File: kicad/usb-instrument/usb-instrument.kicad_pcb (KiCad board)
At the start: 4 copper layers, 100 x 100 mm, 74 parts, among them J1 USB_B_Micro, J2 USB_C_Receptacle_USB2.0_14P, Q5 BS170, Q6 BSS84, Q7 BS170, Q8 BS170, U1 XIAO-ESP32-C3-DIP, U12 LM321, U13 LM321, U2 ADS131M02IRUKR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

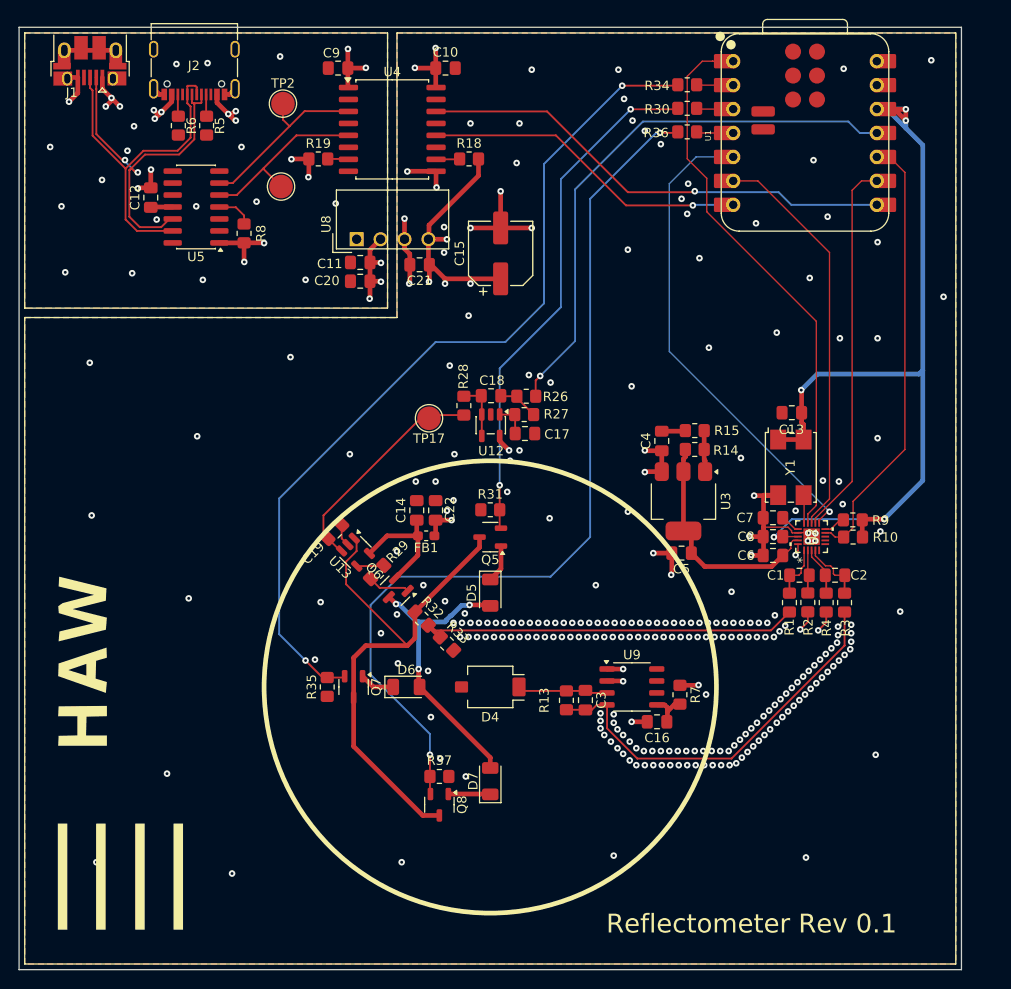
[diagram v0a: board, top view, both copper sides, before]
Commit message: updated footprints
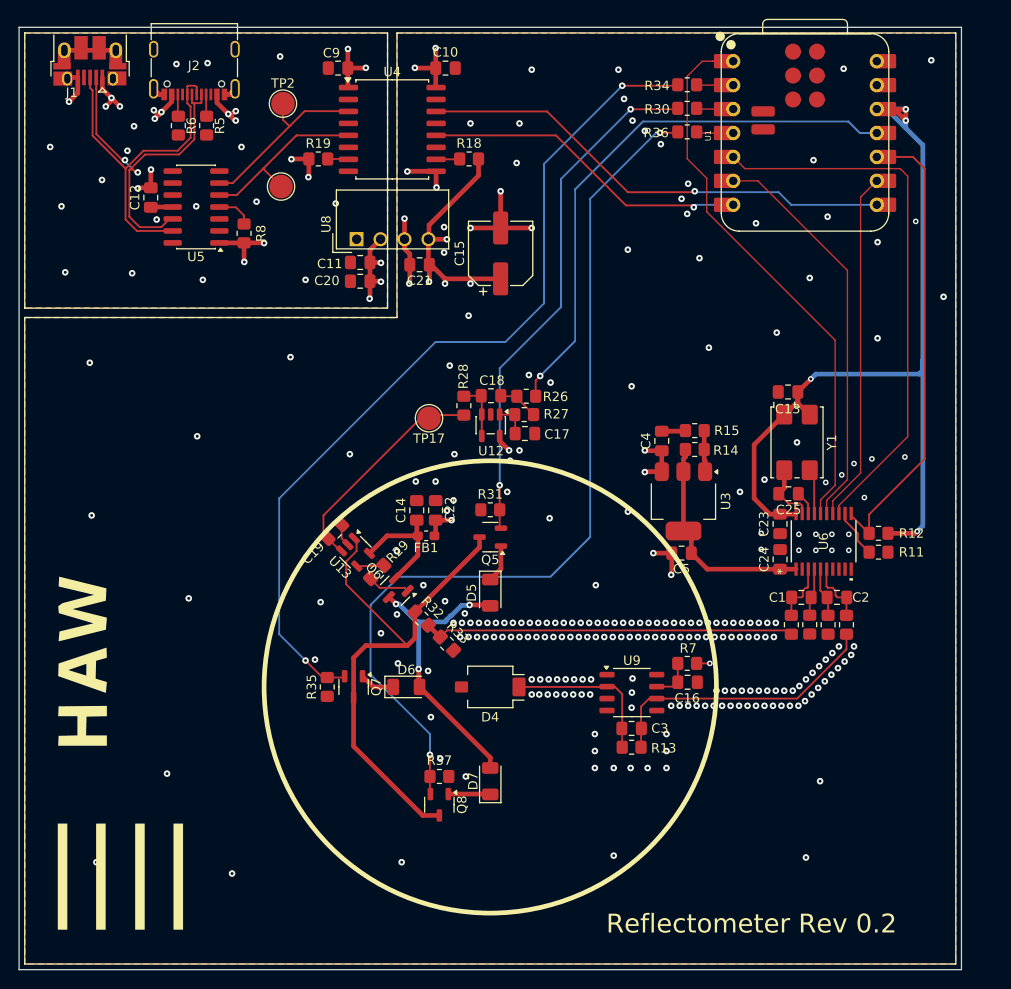
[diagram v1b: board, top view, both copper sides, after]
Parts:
- removed C6, C8: 1u, Capacitor_SMD:C_0805_2012Metric_Pad1.18x1.45mm_HandSolder
- removed C7: 220n, Capacitor_SMD:C_0805_2012Metric_Pad1.18x1.45mm_HandSolder
- removed R10, R9: 10k, Resistor_SMD:R_0805_2012Metric_Pad1.20x1.40mm_HandSolder
- removed U2: ADS131M02IRUKR, Footprints:WQFN20_ADS131_TEX
- added C23: 1u, Capacitor_SMD:C_0805_2012Metric_Pad1.18x1.45mm_HandSolder, F.Cu at (130.8, 102.7)
- added C24: 1u, Capacitor_SMD:C_0805_2012Metric_Pad1.18x1.45mm_HandSolder, F.Cu at (130.8, 106.5)
- added C25: 220n, Capacitor_SMD:C_0805_2012Metric_Pad1.18x1.45mm_HandSolder, F.Cu at (131.7, 99.5)
- added R11: 10k, Resistor_SMD:R_0805_2012Metric_Pad1.20x1.40mm_HandSolder, F.Cu at (141.2, 105.7)
- added R12: 10k, Resistor_SMD:R_0805_2012Metric_Pad1.20x1.40mm_HandSolder, F.Cu at (141.2, 103.7)
- added U6: ADS131M02IPWR, Footprints:TSSOP20_PW_TEX, F.Cu at (135.4, 104.5)
- moved R13 8.52 mm to (115.0, 126.4), turned to 0 degrees
- moved C3 5.75 mm to (115.0, 124.4), turned to 0 degrees
- moved C16 5.30 mm to (120.9, 119.5), turned to 0 degrees
- moved R7 3.41 mm to (120.9, 117.5), turned to 180 degrees
- moved Y1 2.73 mm to (132.6, 94.0)
- moved C1 2.36 mm to (133.0, 110.5)
- moved C2 2.36 mm to (136.8, 110.5)
- moved R1 2.36 mm to (131.9, 113.4)
- moved R2 2.36 mm to (133.9, 113.4)
- moved R3 2.36 mm to (137.8, 113.4)
- moved R4 2.36 mm to (135.8, 113.4)
- moved C13 2.24 mm to (131.6, 88.7)
- moved U9 0.60 mm to (115.0, 120.6)
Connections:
- U9 pad 1: GNDA -> (no net)
- U9 pad 2: GNDA -> Net-(D4-K)
- U9 pad 3: Net-(D4-K) -> GNDA
- U9 pad 4: /INPUT_STAGE/V_PD -> GNDA
- U9 pad 5: /INPUT_STAGE/5V_OP -> (no net)
- U9 pad 6: (no net) -> /INPUT_STAGE/V_PD
- U9 pad 7: (no net) -> /INPUT_STAGE/5V_OP
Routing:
- net GNDA: track 61.3 -> 38.1 mm, vias 264 -> 246
- net /INPUT_STAGE/V_PD: track 42.1 -> 30.3 mm
- net Net-(D4-K): track 9.65 -> 16.9 mm
- net /GPIO6: track 51.7 -> 58.2 mm, vias 1 -> 0
- net Net-(U6-*CS): track 0.00 -> 5.16 mm
- net /ESP_SCK: track 40.0 -> 37.2 mm
- net Net-(U6-CAP): track 0.00 -> 2.58 mm
- net /SYNC/RESET: track 46.4 -> 48.8 mm
- net Net-(U2-CS): track 2.33 -> 0.00 mm
- net Net-(U2-CAP): track 2.00 -> 0.00 mm
- net /INPUT_STAGE/CLKIN: track 2.97 -> 4.79 mm
- net /INPUT_STAGE/AVDD: track 24.7 -> 23.2 mm
- net /ESP_3.3V: track 99.0 -> 97.7 mm, vias 5 -> 4
- net /INPUT_STAGE/R_SENSE: track 40.4 -> 39.5 mm
- net VCCQ: track 46.1 -> 45.5 mm
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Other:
- board text added: "Reflectometer Rev 0.2"
- board text removed: "Reflectometer Rev 0.1"
